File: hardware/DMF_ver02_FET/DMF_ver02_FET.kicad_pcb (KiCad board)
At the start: 2 copper layers, 44 parts, among them J1 GND_Electrodes, J10 GND, J2 POWER, J3 GND_Electrodes, J4 Ard_1, J5 Ard_2, J6 Ard_3, J7 Ard_4, J8 Ard_5, J9 Ard_6, Q1 IRF740, Q2 IRF740, Q3 IRF740, Q4 IRF740, Q5 IRF740, Q6 IRF740

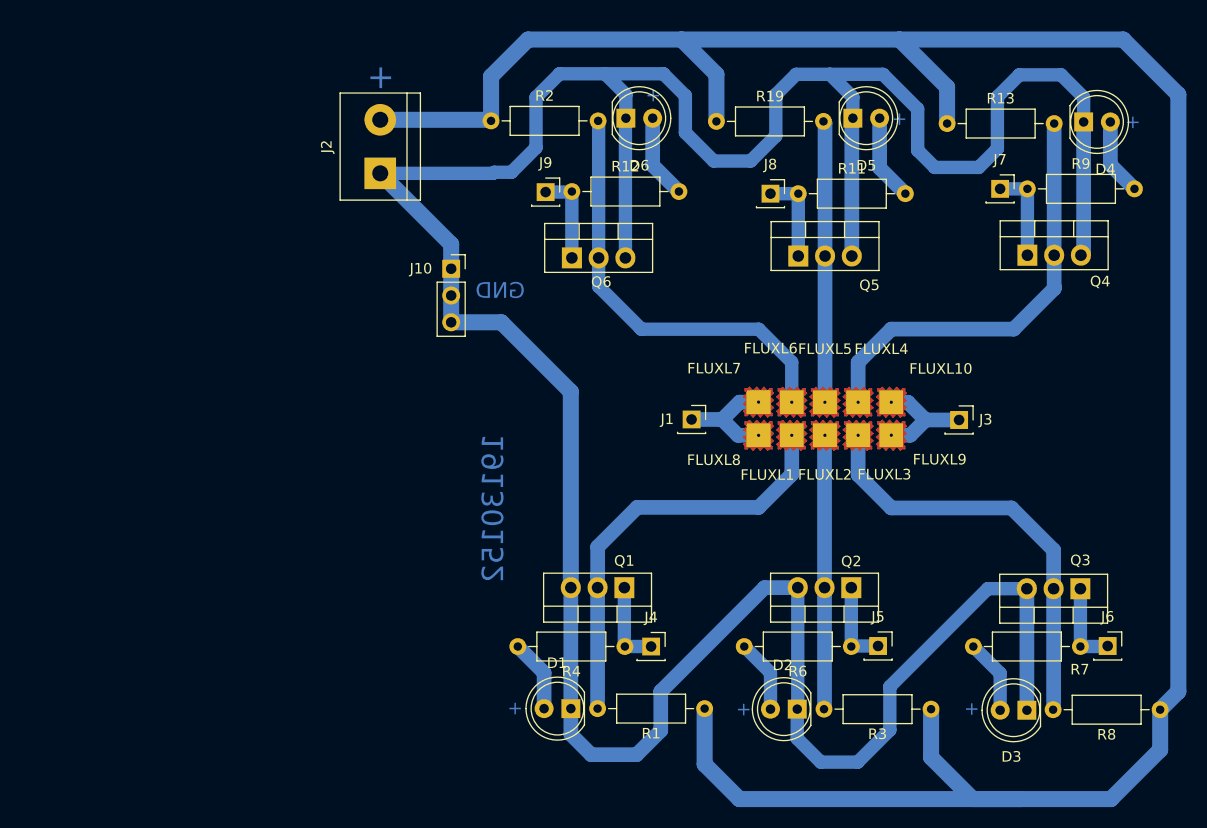
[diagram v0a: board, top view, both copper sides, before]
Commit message: Create DMF board version SMD
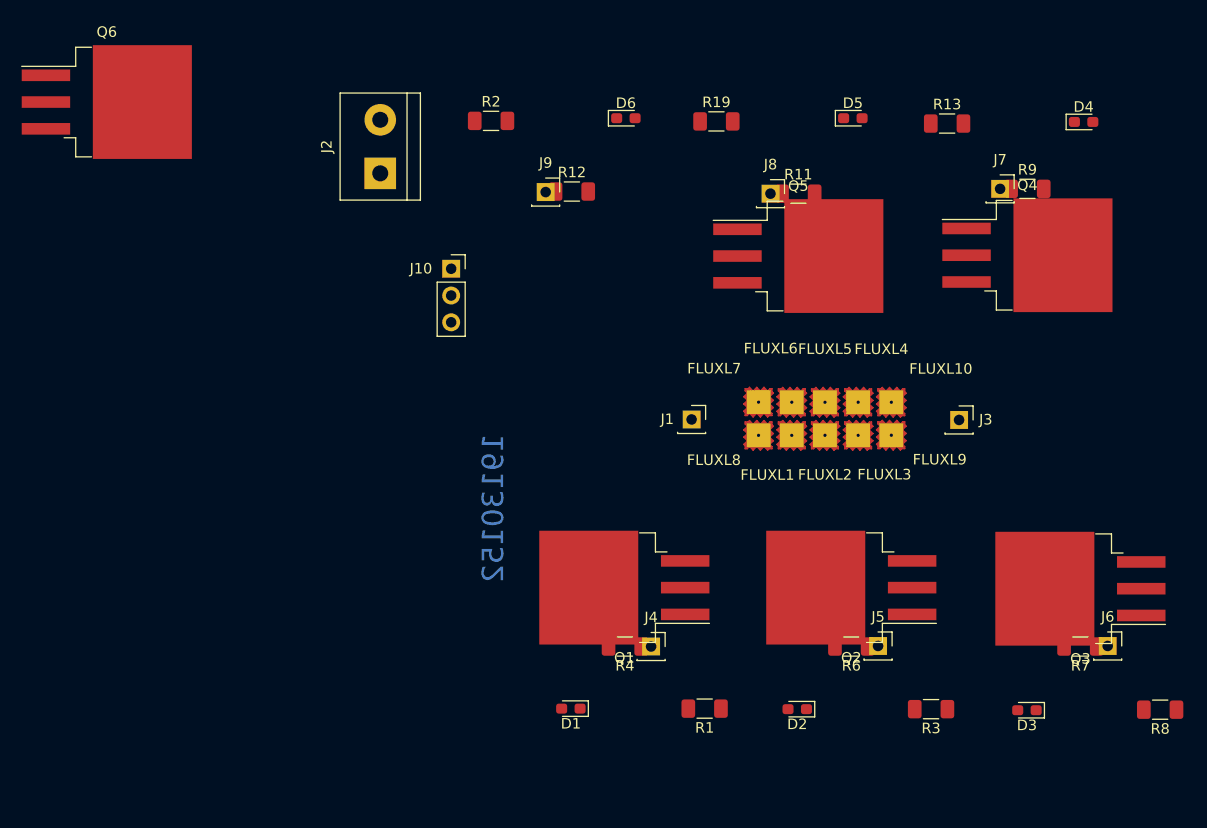
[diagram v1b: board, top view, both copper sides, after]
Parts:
- D1, D2, D3, D4, D5, D6: footprint LED_THT:LED_D5.0mm_IRBlack -> LED_SMD:LED_0603_1608Metric_Pad1.05x0.95mm_HandSolder
- Q1, Q2, Q3, Q4, Q5, Q6: footprint Package_TO_SOT_THT:TO-220-3_Vertical -> Package_TO_SOT_SMD:TO-263-3_TabPin2
- R1, R11, R12, R13, R19, R2, R3, R4, R6, R7, R8, R9: footprint Resistor_THT:R_Axial_DIN0207_L6.3mm_D2.5mm_P10.16mm_Horizontal -> Resistor_SMD:R_1206_3216Metric_Pad1.30x1.75mm_HandSolder
- moved Q6 46.6 mm to (43.7, 75.5)
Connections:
- net /LED_6 renamed /pin_6
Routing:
- net GND: track 302.0 -> 0.00 mm
- net /+HV: track 232.1 -> 0.00 mm
- net /PAD_4: track 41.0 -> 0.00 mm
- net /PAD_6: track 40.8 -> 0.00 mm
- net /PAD_3: track 40.4 -> 0.00 mm
- net /PAD_1: track 40.3 -> 0.00 mm
- net /PAD_5: track 26.7 -> 0.00 mm
- net /PAD_2: track 26.1 -> 0.00 mm
- net Net-(FLUXL7-Pad1): track 11.1 -> 0.00 mm
- net Net-(FLUXL10-Pad1): track 11.0 -> 0.00 mm
- net /LED_4: track 8.89 -> 0.00 mm
- net /pin_6: track 8.81 -> 0.00 mm
- net /LED_5: track 8.56 -> 0.00 mm
- net Net-(D5-Pad2): track 8.17 -> 0.00 mm
- net /LED_2: track 8.15 -> 0.00 mm
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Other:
- board text removed: "+"
- board text removed: "GND"

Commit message: Update PCB layout: Placed components.
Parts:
- removed J10: GND, Connector_PinSocket_2.54mm:PinSocket_1x03_P2.54mm_Vertical
- removed J5: Ard_2, Connector_PinSocket_2.54mm:PinSocket_1x01_P2.54mm_Vertical
- removed J6: Ard_3, Connector_PinSocket_2.54mm:PinSocket_1x01_P2.54mm_Vertical
- removed J7: Ard_4, Connector_PinSocket_2.54mm:PinSocket_1x01_P2.54mm_Vertical
- removed J8: Ard_5, Connector_PinSocket_2.54mm:PinSocket_1x01_P2.54mm_Vertical
- removed J9: Ard_6, Connector_PinSocket_2.54mm:PinSocket_1x01_P2.54mm_Vertical
- J4: value Ard_1 -> Conn_01x09_Female; footprint Connector_PinSocket_2.54mm:PinSocket_1x01_P2.54mm_Vertical -> Connector_PinHeader_2.54mm:PinHeader_1x09_P2.54mm_Vertical
- moved Q6 56.8 mm to (99.2, 87.8), turned to -90 degrees
- moved R9 54.0 mm to (85.0, 111.9)
- moved R7 52.7 mm to (85.0, 114.5), turned to 0 degrees
- moved R11 35.0 mm to (85.0, 109.4)
- moved J4 32.0 mm to (79.7, 99.2)
- moved R6 31.1 mm to (85.0, 117.0), turned to 0 degrees
- moved R12 23.1 mm to (85.0, 106.9)
- moved R8 19.0 mm to (124.8, 134.7), turned to 90 degrees
- moved R2 19.0 mm to (99.2, 76.5), turned to -90 degrees
- moved D4 14.2 mm to (122.3, 76.5), turned to 90 degrees
- moved J2 14.2 mm to (82.1, 89.1)
- moved D1 13.9 mm to (101.6, 134.6), turned to -90 degrees
- moved Q3 11.6 mm to (124.7, 123.7), turned to 90 degrees
- moved R4 10.9 mm to (85.0, 119.5), turned to 0 degrees
- moved R19 10.4 mm to (112.0, 76.5), turned to -90 degrees
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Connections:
- J4 pad 1: /LED_1 -> GND
- Q6 pad 1: /pin_6 -> /LED_6
- R12 pad 1: /pin_6 -> /LED_6
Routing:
- net /PAD_2: track 0.00 -> 22.3 mm, vias 0 -> 1
- net /PAD_1: track 0.00 -> 9.15 mm
- net /PAD_3: track 0.00 -> 9.15 mm
- net /LED_5: track 0.00 -> 3.79 mm
- net /LED_6: track 0.00 -> 3.78 mm
- net /LED_1: track 0.00 -> 3.78 mm
- net /LED_3: track 0.00 -> 3.78 mm
- net /LED_4: track 0.00 -> 3.77 mm
- net /LED_2: track 0.00 -> 3.76 mm
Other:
- board text added: "19130152 Huynh Giao"
- board text removed: "19130152"
